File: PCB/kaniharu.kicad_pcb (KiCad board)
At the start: 4 copper layers, 75 x 50 mm, 97 parts, among them J1 Conn_01x04, J2 USB_C_Receptacle_USB2.0_14P, J3 Conn_02x03_Odd_Even, J4 Conn_02x03_Odd_Even, J6 RJ45_Pulse_JXD6-0001NL, J7 USB_C_Receptacle_USB2.0_14P, SW1 SW_Push, U1 STM32H723VGTx, U2 ISO1044BD, U3 ISO1044BD, U4 AZ1117-3.3, U6 DP83848C, Y1 CSTNE16M0V53C000R0, Y2 50M

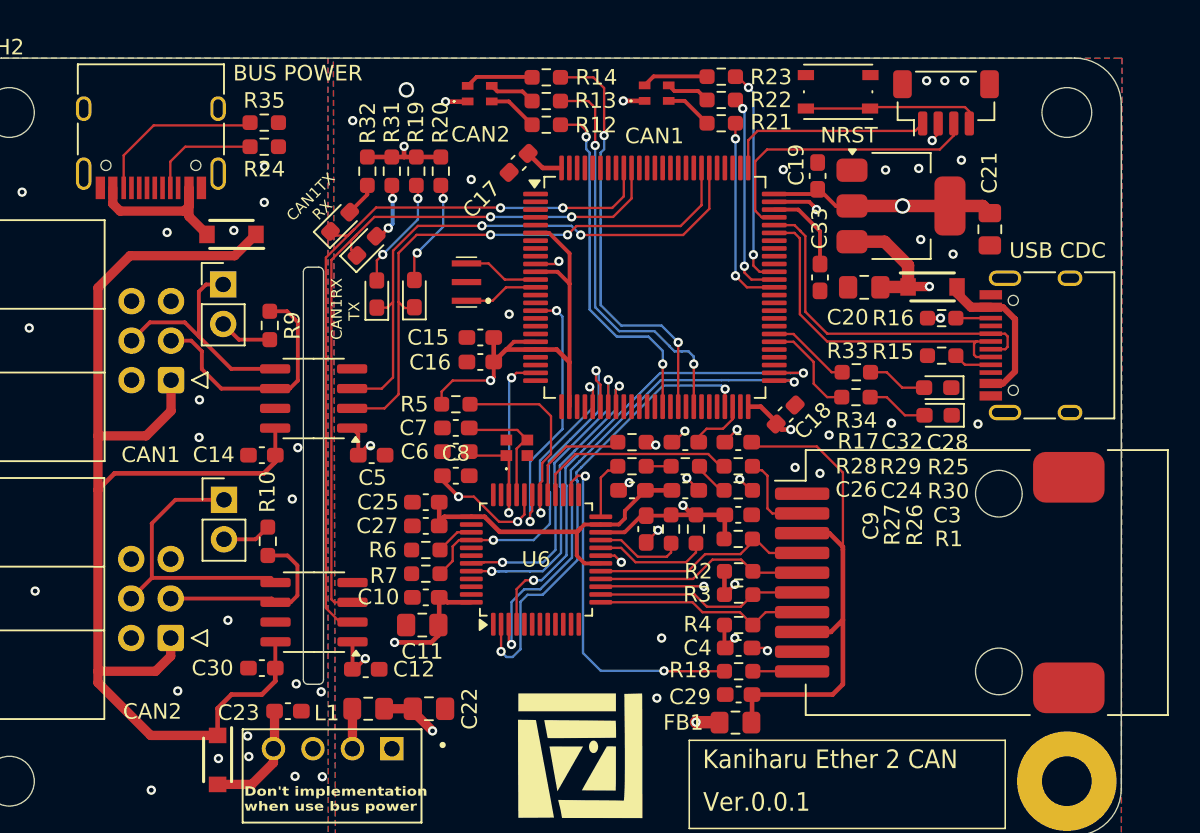
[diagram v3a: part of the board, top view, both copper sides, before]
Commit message: update:基板発注した
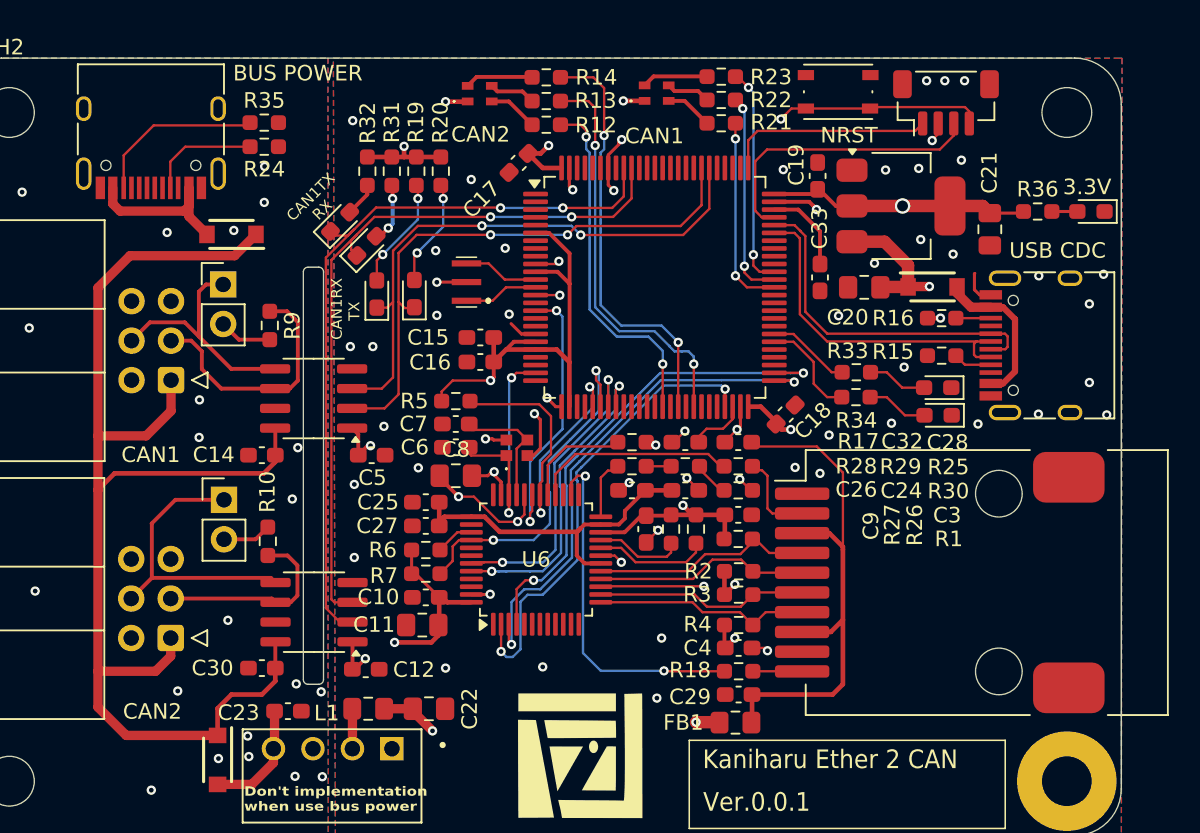
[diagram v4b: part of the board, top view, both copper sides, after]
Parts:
- added D10: LED, LED_SMD:LED_0603_1608Metric_Pad1.05x0.95mm_HandSolder, F.Cu at (173.1, 89.9)
- added R36: 10k, Resistor_SMD:R_0603_1608Metric_Pad0.98x0.95mm_HandSolder, F.Cu at (169.6, 89.9)
- C20, C21: value C -> 10u
- C3, C4: value C_Small -> 100n
- C8: footprint Capacitor_SMD:C_0603_1608Metric_Pad1.08x0.95mm_HandSolder -> Capacitor_SMD:C_0805_2012Metric_Pad1.18x1.45mm_HandSolder
- R12, R13, R14, R17, R18, R19, R20, R21, R22, R23, R25, R31, R32, R33, R34: value R -> 10k
- R26, R27: value R -> 2.2k
- moved C6 0.28 mm to (132.2, 105.0)
- moved C7 0.25 mm to (132.2, 103.5)
- moved R5 0.20 mm to (132.2, 102.1)
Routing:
- net NRST: track 11.4 -> 36.6 mm, vias 0 -> 2
- net GND: track 22.3 -> 45.5 mm, vias 32 -> 61
- net +3.3V: track 242.8 -> 255.5 mm
- net Net-(D10-A): track 0.00 -> 1.64 mm
- net /ETH/ETH_TXD0: track 34.3 -> 33.1 mm
- net +5VA: track 82.7 -> 83.6 mm
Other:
- board text added: "3.3V"
